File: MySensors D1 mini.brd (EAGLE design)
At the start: 27.1 x 36.1 mm, 24 parts, among them IC1 MEGA328P-AU, IC2 AT25DF512C-SSHN-B, IC3 REG1117, IC4 ATSHA204A, M1 WIRELESS-NRF24L01SMD, Q1 N/M

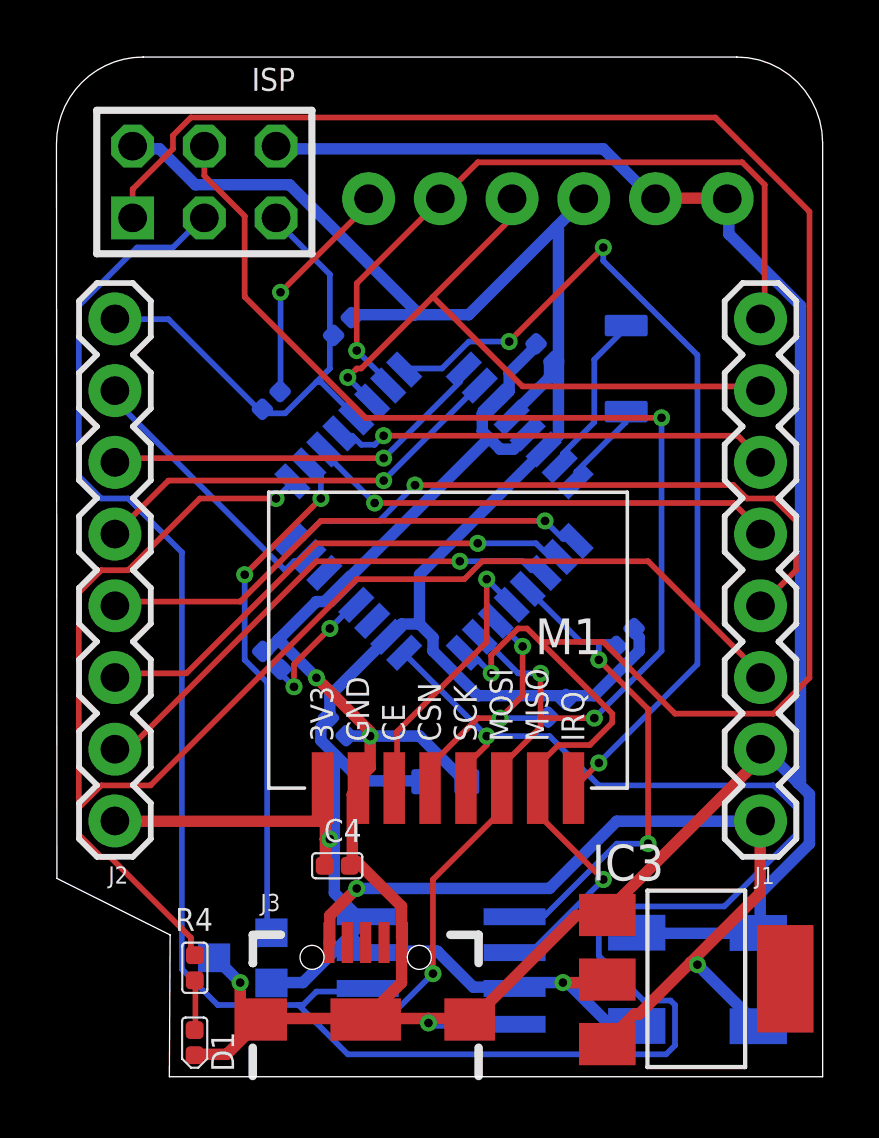
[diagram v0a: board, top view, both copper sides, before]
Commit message: Updated labels, fixed issue with MicroUSB
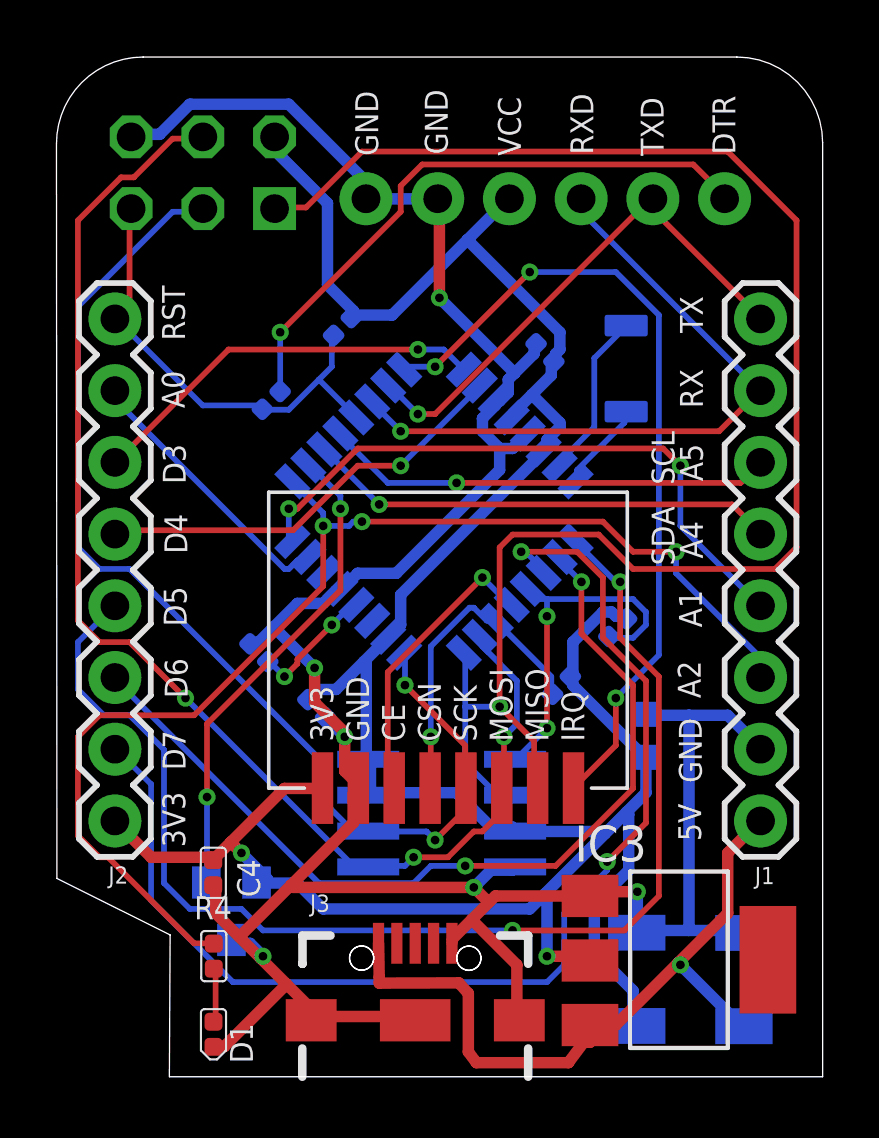
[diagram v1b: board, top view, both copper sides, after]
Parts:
- moved JP2 12.8 mm to (11.0, 31.1), flipped to the bottom
- moved C3 7.31 mm to (20.9, 12.1), turned to 270 degrees
- moved IC2 5.57 mm to (13.6, 9.34)
- moved C4 4.40 mm to (5.56, 7.22), turned to 270 degrees
- moved J3 1.76 mm to (12.7, 2.00)
- moved IC4 1.70 mm to (6.20, 5.86), turned to 180 degrees
- moved C6 0.98 mm to (9.22, 13.0)
- moved IC3 0.91 mm to (22.0, 4.14)
- moved R6 0.82 mm to (17.9, 13.9)
- moved R4 0.79 mm to (5.57, 4.27)
- moved D1 0.73 mm to (5.56, 1.50)
- moved C2 0.53 mm to (7.17, 15.0)
- moved C8 0.51 mm to (24.3, 3.44)
- moved R5 0.44 mm to (19.9, 15.9)
- moved JP3 0.33 mm to (5.19, 32.0), flipped to the bottom
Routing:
- net SCK: track 86.6 -> 40.2 mm, vias 1 -> 2
- net D5: track 17.8 -> 44.8 mm, vias 1 -> 2
- net D7: track 18.1 -> 42.0 mm, vias 1 -> 2
- net MISO: track 76.0 -> 59.9 mm, vias 2 -> 1
- net GND: track 122.3 -> 106.9 mm, vias 4 -> 6
- net D6: track 17.9 -> 32.0 mm, vias 1 -> 2
- net DTR: track 8.16 -> 21.4 mm
- net A2: track 53.5 -> 43.7 mm, vias 1 -> 3
- net MOSI: track 53.9 -> 46.3 mm, vias 4 -> 3
- net TXD: track 25.4 -> 19.0 mm
- net +5V: track 31.2 -> 25.8 mm, vias 2 -> 1
- net D8: track 17.6 -> 12.6 mm
- net V+: track 98.3 -> 101.3 mm
- net D2: track 31.2 -> 29.1 mm
- net D10: track 9.86 -> 11.5 mm, vias 2 -> 1
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
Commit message: Add files via upload
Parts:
- moved C3 2.02 mm to (20.7, 10.1)
- moved C7 0.65 mm to (19.9, 3.39)
- moved D1 0.55 mm to (6.10, 1.60)
- moved C4 0.51 mm to (6.06, 7.22)
- moved R4 0.51 mm to (6.08, 4.27)
- moved IC4 0.27 mm to (6.47, 5.91)
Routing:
- net D5: track 44.8 -> 24.3 mm, vias 2 -> 1
- net DTR: track 21.4 -> 38.1 mm, vias 1 -> 0
- net D6: track 32.0 -> 43.8 mm
- net MISO: track 59.9 -> 68.1 mm, vias 1 -> 2
- net A2: track 43.7 -> 51.5 mm
- net V+: track 101.3 -> 95.5 mm
- net +5V: track 25.8 -> 30.6 mm, vias 1 -> 0
- net D8: track 12.6 -> 16.5 mm, vias 2 -> 0
- net TXD: track 19.0 -> 22.7 mm
- net RXD: track 24.2 -> 21.7 mm
- net D7: track 42.0 -> 40.3 mm, vias 2 -> 5
- net D10: track 11.5 -> 9.88 mm
- net GND: track 106.9 -> 105.9 mm, vias 6 -> 5
- net A1: track 22.4 -> 23.3 mm, vias 2 -> 1
- net D9: track 10.4 -> 9.60 mm
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
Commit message: Add files via upload
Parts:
- moved IC4 0.76 mm to (6.13, 5.24)
- moved C7 0.25 mm to (19.7, 3.42)
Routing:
- net V+: track 95.5 -> 118.2 mm
- net MOSI: track 46.3 -> 65.1 mm
- net D7: track 40.3 -> 21.8 mm, vias 5 -> 1
- net MISO: track 68.1 -> 50.5 mm, vias 2 -> 3
- net D2: track 28.6 -> 43.8 mm, vias 3 -> 1
- net D5: track 24.3 -> 37.2 mm
- net D6: track 43.8 -> 31.0 mm
- net A1: track 23.3 -> 34.0 mm, vias 1 -> 2
- net A2: track 51.5 -> 61.9 mm, vias 3 -> 2
- net DTR: track 38.1 -> 28.7 mm
- net GND: track 105.9 -> 111.3 mm, vias 5 -> 3
- net RXD: track 21.7 -> 20.9 mm
- net N$4: track 3.96 -> 4.57 mm, vias 0 -> 2
- net D9: track 9.60 -> 10.2 mm

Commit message: Add files via upload
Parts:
- moved IC4 1.61 mm to (7.21, 4.05)
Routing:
- net D5: track 37.2 -> 18.6 mm
- net V+: track 118.2 -> 100.0 mm, vias 2 -> 1
- net A1: track 34.0 -> 19.7 mm, vias 2 -> 1
- net D6: track 31.0 -> 17.8 mm, vias 2 -> 1
- net A3: track 17.3 -> 27.5 mm
- net MOSI: track 65.1 -> 54.9 mm, vias 3 -> 2
- net A2: track 61.9 -> 52.8 mm
- net MISO: track 50.5 -> 45.5 mm
- net SCK: track 40.9 -> 45.9 mm
- net D8: track 16.4 -> 12.6 mm, vias 0 -> 2
- net TXD: track 22.4 -> 18.7 mm
- net GND: track 111.3 -> 109.0 mm, vias 3 -> 4
- net D7: track 21.8 -> 19.6 mm, vias 1 -> 2
- net D10: track 9.88 -> 11.5 mm
- net RXD: track 20.9 -> 21.8 mm
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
